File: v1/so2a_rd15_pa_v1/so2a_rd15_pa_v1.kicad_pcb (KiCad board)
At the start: 2 copper layers, 90 x 50.9 mm, 60 parts, among them J1 RF_in, J2 RF_out, Q1 RD15HVF1, Q2 MMBT3904, U1 L78L05_SOT89

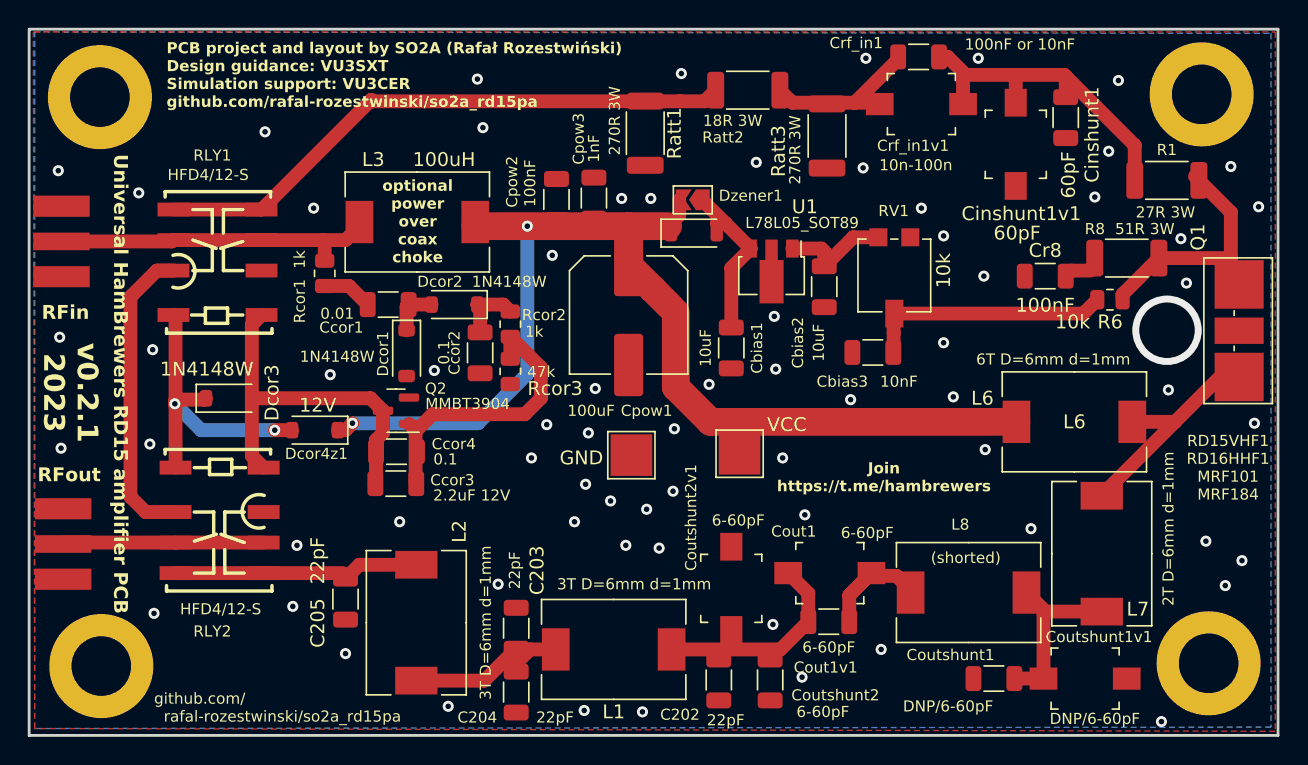
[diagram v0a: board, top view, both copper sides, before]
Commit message: v0.3.1: Adding minimal board; changes for the drain trace width
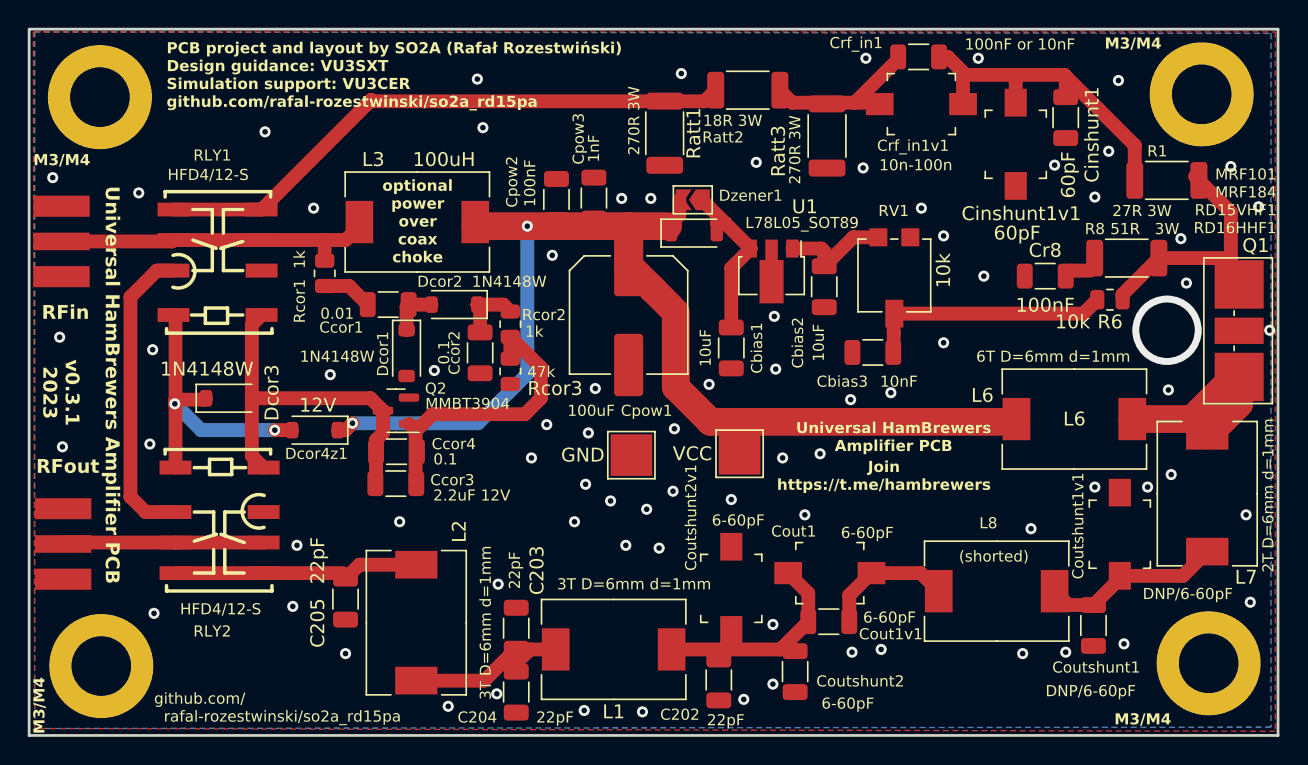
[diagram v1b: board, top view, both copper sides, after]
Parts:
- R8: value 51R 3W -> 51R 3W
- moved Coutshunt1v1 10.7 mm to (180.2, 86.1), turned to 90 degrees
- moved L7 8.74 mm to (186.5, 83.2)
- moved Coutshunt1 8.13 mm to (178.3, 92.7), turned to 90 degrees
- moved L8 2.03 mm to (171.3, 90.2)
- moved Coutshunt2 1.90 mm to (156.8, 96.0)
- moved Ratt1 1.40 mm to (147.4, 57.2)
- moved L6 0.20 mm to (176.9, 77.8)
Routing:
- net Drain: track 16.3 -> 18.8 mm
- net GND: vias 71 -> 80
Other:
- board text added: "Bias"
- board text added: "Carrier Operated Relay"
- board text added: "Input match/L-match"
- board text added: "Low Pass Filter"
- board text added: "M3/M4"
- board text added: "MRF101 MRF184 RD15VHF1 RD16HHF1"
- board text added: "Optional Attenuator"
- board text added: "Output L-match network"
- board text added: "Universal HamBrewers Amplifier PCB"
- board text added: "Universal HamBrewers amplifier PCB https://github.com/rafal-rozestwinski/so2a_rd15pa PCB project and layout by SO2A (Rafał Rozestwiński) Design guidance: VU3SXT Simulation support: VU3CER Join https://t.me/hambrewers No warranty, (C) not for commercial purposes v0.3.1 2023"
- board text added: "v0.3.1 2023"
- board text removed: "RD15VHF1 RD16HHF1 MRF101 MRF184"
- board text removed: "Universal HamBrewers RD15 amplifier PCB"
- board text removed: "Universal HamBrewers amplifier PCB https://github.com/rafal-rozestwinski/so2a_rd15pa PCB project and layout by SO2A (Rafał Rozestwiński) Design guidance: VU3SXT Simulation support: VU3CER Join https://t.me/hambrewers No warranty, (C) not for commercial purposes v0.2.1 2023"
- board text removed: "v0.2.1 2023"
